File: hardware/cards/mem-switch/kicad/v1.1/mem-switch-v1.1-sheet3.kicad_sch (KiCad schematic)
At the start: 8 parts, among them IC1 74*27, IC2 74*138, IC3 74*138, IC4 74*85, SW1 SW_DIP-4

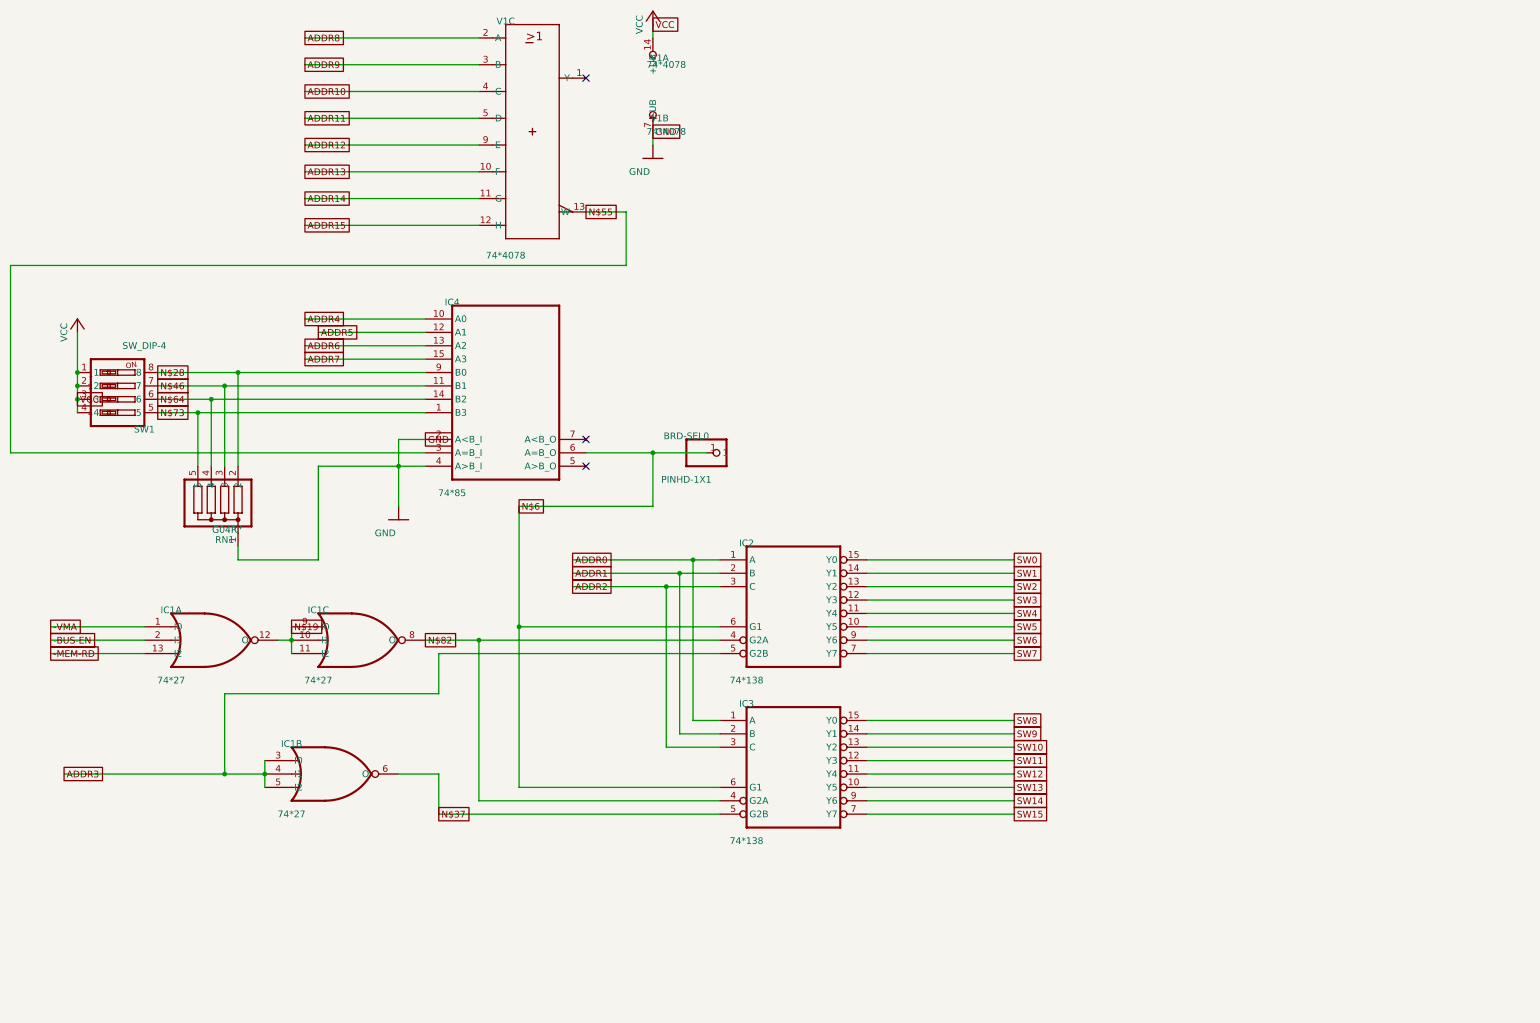
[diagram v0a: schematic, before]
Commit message: fix(kicad): readable converted schematics - overlaps 42,847 -> 3,147, nothing off the frame; CF sheet 0 overlaps
- tools/kicad/sch_overlaps.py: calibrated readability check (text/text, text/body, text/line, off frame/title block)
- eagle_sch_to_kicad.py: fields placed from Eagle's smashed attributes or the symbol's >NAME/>VALUE with Eagle's align,
  size and ratio, readable angles; fields Eagle never shows hidden (FABC96R shows only its pin name); pin numbers hidden
  where every Eagle pin hides them; Eagle-hidden layers dropped (the stray SpiceOrder text); labels on their own wires,
  converter labels only where KiCad needs them; rotate-then-mirror fixed for MR90/MR270 in pin_world/no-connects;
  each sheet on the smallest page that holds it, centred clear of the title block
- finish_board.py: stable footprint-library choice (DRC counts no longer vary run to run)
- all 37 projects regenerated: netlist proofs unchanged (34 MATCH, 2 schematic-only, video Fusion export MISMATCH as
  before); DRC same or better; ERC up (loose wire ends onto graphic buses no longer hidden by labels; explained per README)
- CF card: gate names off the gate bodies, U3 clear of its title, 5.08 mm connector pins; rebuilt: DRC 0/0, proof MATCH
- schematic PDFs regenerated (tools/sch_to_pdf.py, 37/37)

Co-Authored-By: Claude Opus 5.5 <noreply@anthropic.com>
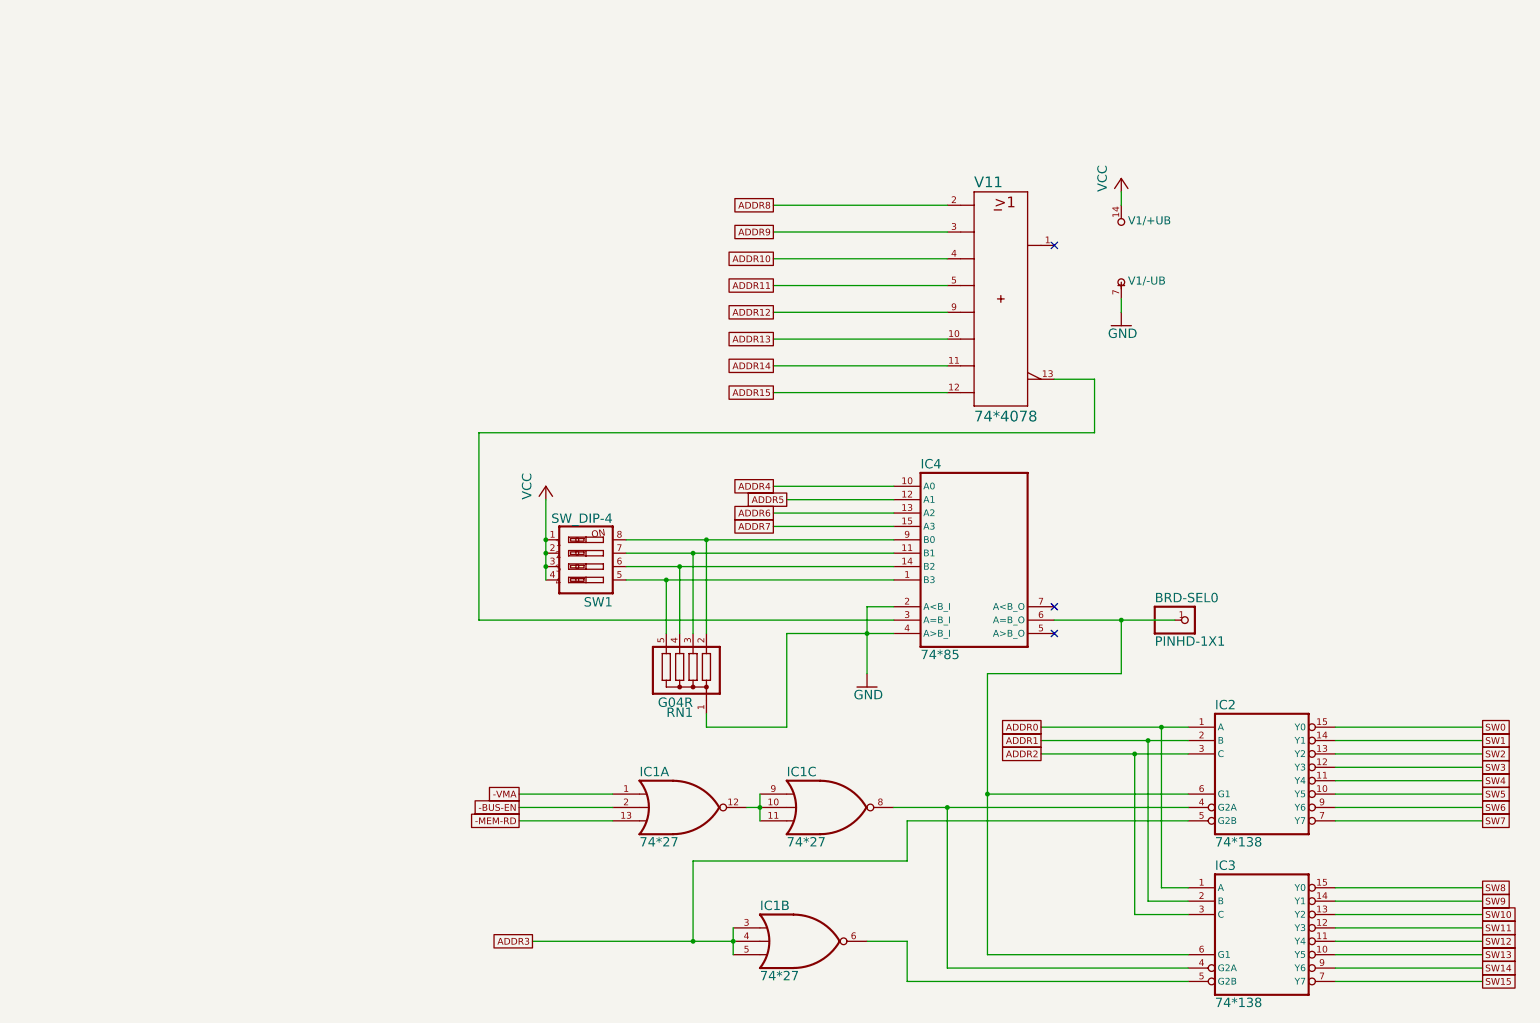
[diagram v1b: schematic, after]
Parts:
- V1: Eagle name (none) -> V1/+UB
- V1: Eagle name (none) -> V11
- V1: Eagle name (none) -> V1/-UB
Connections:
- net N$19: no longer names the net of IC1.10 (I1), IC1.11 (I2), IC1.12 (O), IC1.9 (I0)
- net N$28: no longer names the net of IC4.9 (B0), RN1.2, SW1.8
- net N$37: no longer names the net of IC1.6 (O), IC3.5 (G2B)
- net N$46: no longer names the net of IC4.11 (B1), RN1.3, SW1.7
- net N$55: no longer names the net of IC4.3 (A=B_I), V1.13 (W)
- net N$6: no longer names the net of BRD-SEL0.1, IC2.6 (G1), IC3.6 (G1), IC4.6 (A=B_O)
- net N$64: no longer names the net of IC4.14 (B2), RN1.4, SW1.6
- net N$73: no longer names the net of IC4.1 (B3), RN1.5, SW1.5
- net N$82: no longer names the net of IC1.8 (O), IC2.4 (G2A), IC3.4 (G2A)
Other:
- moved on the sheet: IC2, IC3, IC4
